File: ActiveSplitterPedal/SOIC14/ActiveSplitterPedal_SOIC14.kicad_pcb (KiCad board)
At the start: 2 copper layers, 124 x 100.8 mm, 78 parts, among them J1 MonoJack2Switch, J2 MonoJack2Switch, J3 MonoJack2Switch, J4 MonoJack2Switch, J5 MonoJack2Switch, J6 Barrel_Jack, U1 TL074, U2 TL074, U3 TL074, U4 TL074, U5 TPS60400, U6 TPS60400, U7 TPS60400, U8 TPS60400, U9 SE8250X2

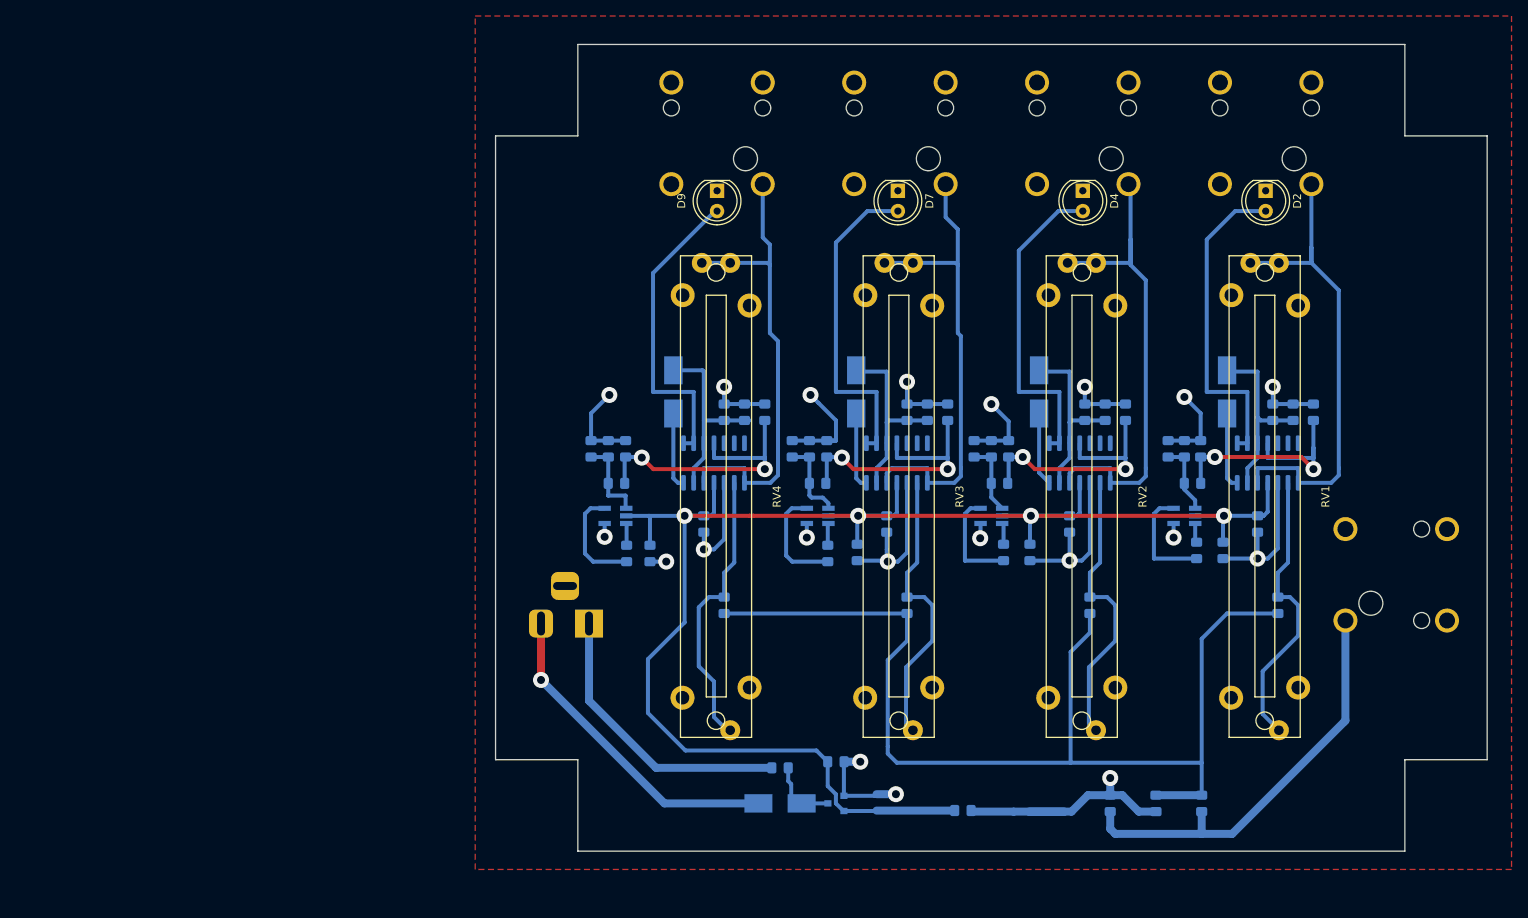
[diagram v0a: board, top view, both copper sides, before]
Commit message: Adjusted layout edges using Hammond 1590BB outline
- Moved components to fit within reduced board area
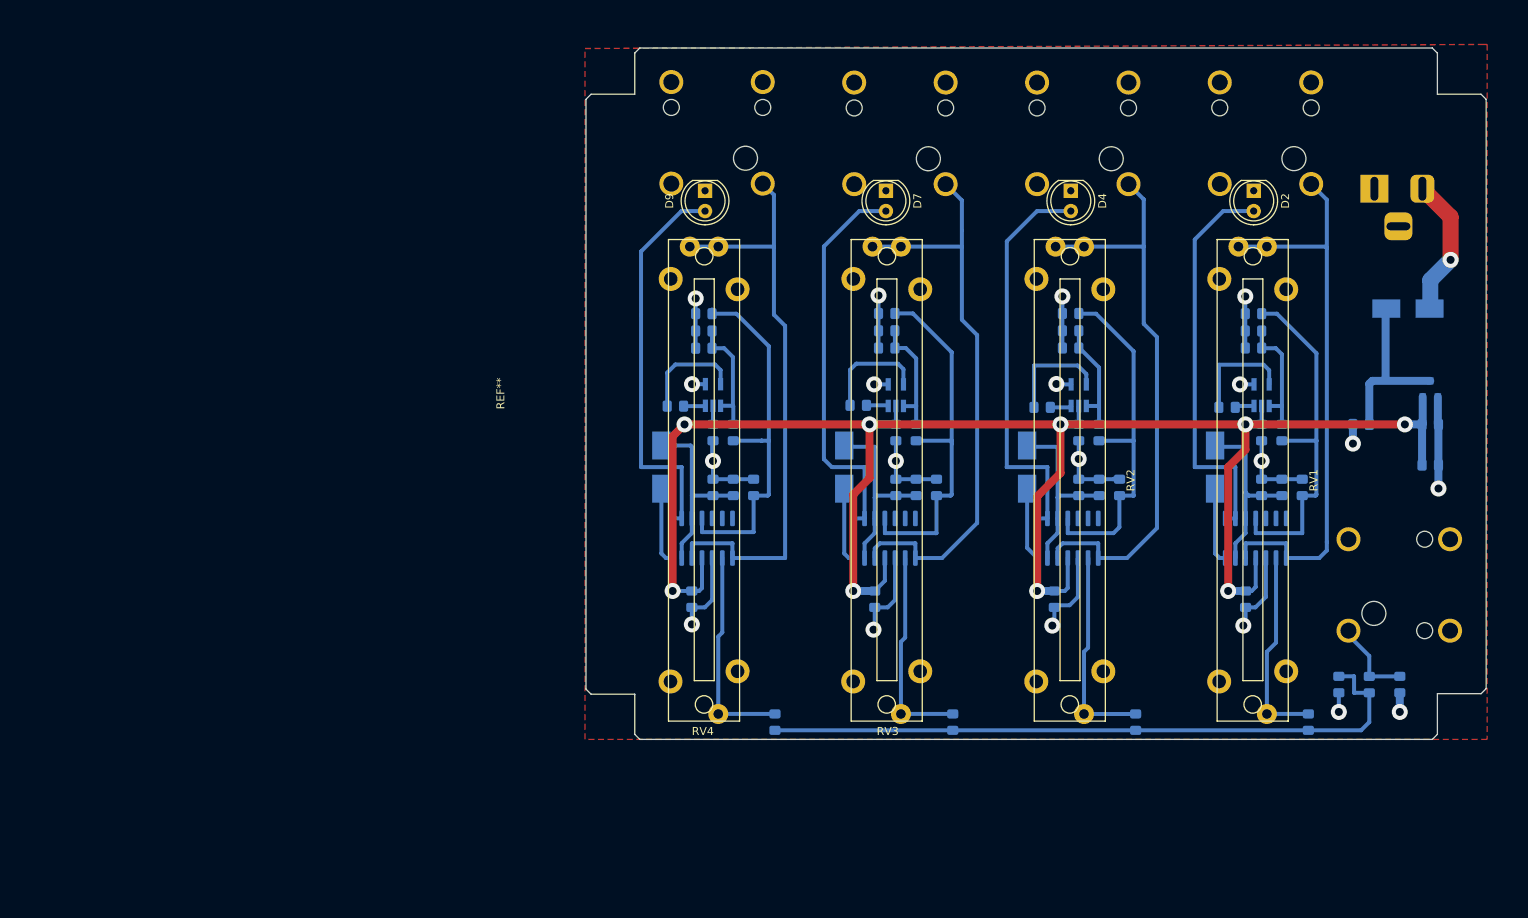
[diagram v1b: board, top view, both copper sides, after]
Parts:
- added REF**: 1590BB, Hammond1590:1590BB, F.Cu at (207.3, 67.6)
- moved J6 112.2 mm to (249.6, 41.9), turned to 180 degrees
- moved D5 99.9 mm to (253.7, 56.9), turned to 0 degrees
- moved U9 90.6 mm to (256.5, 66.9), turned to 90 degrees
- moved C5 84.4 mm to (247.9, 71.4)
- moved C8 83.0 mm to (256.5, 76.5)
- moved C10 75.8 mm to (256.5, 71.4)
- moved R6 39.1 mm to (252.7, 103.9), turned to 270 degrees
- moved R7 27.3 mm to (245.1, 103.9)
- moved R5 25.7 mm to (248.9, 103.9), turned to 90 degrees
- moved C28 19.5 mm to (165.7, 57.5), turned to 180 degrees
- moved U7 19.4 mm to (166.9, 67.7), turned to 90 degrees
- moved C26 19.4 mm to (162.2, 69.1), turned to 180 degrees
- moved C27 19.0 mm to (165.7, 59.7), turned to 180 degrees
- moved C22 18.9 mm to (185.0, 69.0), turned to 180 degrees
- moved C34 18.9 mm to (165.7, 61.8), turned to 180 degrees
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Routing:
- net GNDS: track 233.9 -> 133.5 mm
- net /GainAndPeakDetector1/SIGNAL_INPUT: track 136.7 -> 84.2 mm
- net Net-(J5-Pad1): track 53.0 -> 9.97 mm
- net +5V: track 208.7 -> 238.2 mm, vias 4 -> 9
- net /PowerSupply/+9V_IN: track 40.8 -> 17.1 mm
- net /GainAndPeakDetector4/SIGNAL_OUTPUT: track 59.1 -> 73.8 mm
- net /GainAndPeakDetector3/SIGNAL_OUTPUT: track 59.7 -> 73.3 mm
- net /GainAndPeakDetector2/-5V_POL: track 32.2 -> 45.5 mm, vias 2 -> 0
- net /GainAndPeakDetector3/-5V_POL: track 33.4 -> 46.4 mm, vias 2 -> 0
- net /PowerSupply/+9V_POL: track 9.19 -> 21.7 mm
- net /GainAndPeakDetector1/-5V_POL: track 32.9 -> 45.0 mm, vias 2 -> 0
- net /GainAndPeakDetector2/SIGNAL_OUTPUT: track 61.4 -> 72.7 mm
- net /GainAndPeakDetector4/-5V_POL: track 35.7 -> 46.7 mm, vias 2 -> 0
- net Net-(D9-Pad2): track 38.8 -> 49.8 mm
- net Net-(R1-Pad1): track 36.1 -> 25.2 mm
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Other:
- board size 124 x 100.8 mm -> 112.5 x 86.4 mm

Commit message: updated
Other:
- board text added: "Active 4-Way Splitter RevA"
- board text removed: "Active 4-Way Splitter Hammond 1590BB"

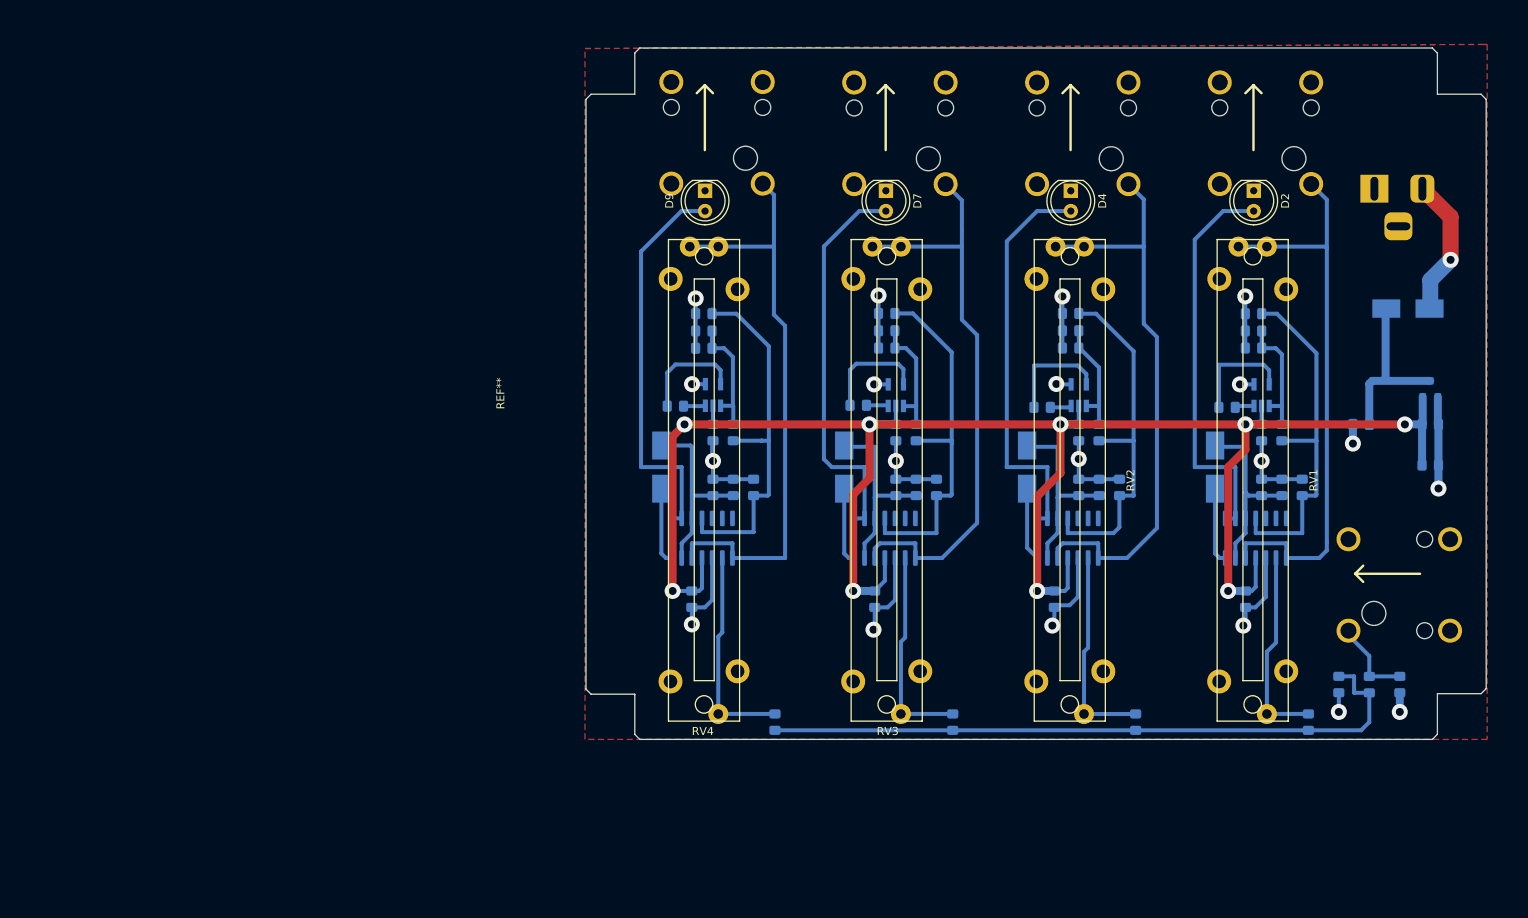
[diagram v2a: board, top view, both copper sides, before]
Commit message: updated RevA layout
Moved components so that faders would be in centred and symmetrical positions
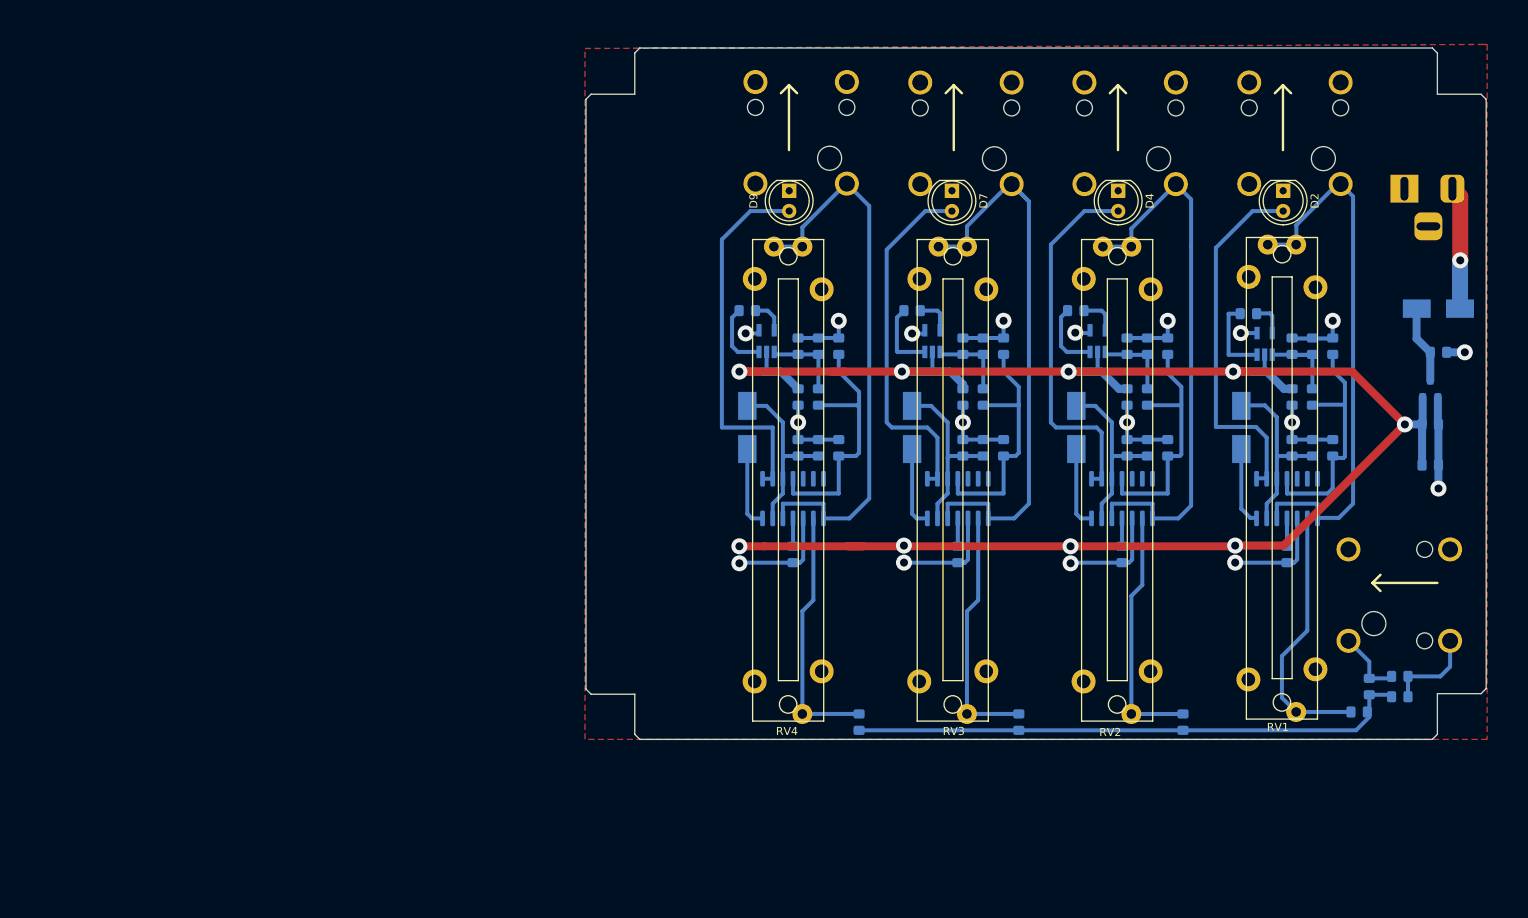
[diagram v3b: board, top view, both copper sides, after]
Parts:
- removed REF**: 1590BB, Hammond1590:1590BB
- moved C28 17.3 mm to (182.6, 61.6), turned to 90 degrees
- moved C24 15.2 mm to (203.2, 61.6), turned to 90 degrees
- moved C26 14.9 mm to (171.2, 57.1), turned to 0 degrees
- moved C27 14.5 mm to (180.1, 61.6), turned to 90 degrees
- moved C18 13.8 mm to (176.9, 87.6)
- moved C22 13.6 mm to (191.8, 57.1), turned to 0 degrees
- moved C5 13.2 mm to (257.6, 62.4), turned to 0 degrees
- moved C11 12.8 mm to (223.7, 61.6), turned to 90 degrees
- moved C2 12.8 mm to (212.2, 57.1), turned to 0 degrees
- moved U4 12.4 mm to (176.9, 80.6)
- moved C33 12.2 mm to (200.7, 61.6), turned to 90 degrees
- moved C30 12.0 mm to (233.8, 57.5), turned to 0 degrees
- moved D6 11.8 mm to (171.2, 71.8)
- moved C15 11.8 mm to (197.5, 87.6)
- moved C34 11.8 mm to (177.5, 61.6), turned to 90 degrees
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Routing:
- net +5V: track 238.2 -> 278.0 mm
- net GNDS: track 133.5 -> 151.3 mm, vias 20 -> 18
- net /GainAndPeakDetector3/-5V_POL: track 46.4 -> 31.9 mm
- net /GainAndPeakDetector1/SIGNAL_INPUT: track 84.2 -> 69.9 mm
- net /GainAndPeakDetector1/-5V_POL: track 45.0 -> 30.8 mm
- net /GainAndPeakDetector2/-5V_POL: track 45.5 -> 31.5 mm
- net /GainAndPeakDetector4/-5V_POL: track 46.7 -> 33.5 mm
- net /PowerSupply/+9V_POL: track 21.7 -> 9.64 mm
- net Net-(C30-Pad2): track 13.7 -> 4.38 mm
- net Net-(C26-Pad2): track 13.3 -> 4.32 mm
- net Net-(C22-Pad2): track 13.6 -> 4.74 mm
- net Net-(C2-Pad2): track 13.5 -> 4.86 mm
- net Net-(R1-Pad1): track 25.2 -> 33.2 mm
- net Net-(C30-Pad1): track 2.42 -> 10.2 mm
- net Net-(C22-Pad1): track 2.76 -> 8.97 mm
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
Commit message: added uv etch layout
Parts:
- D5: footprint Diode_SMD:D_SMB_Handsoldering -> Diode_SMD:D_SOD-123F
- moved D5 1.30 mm to (258.8, 56.6)
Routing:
- net /PowerSupply/+9V_IN: track 15.4 -> 18.7 mm

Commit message: updated reva layout
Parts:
- moved R1 91.5 mm to (158.8, 128.9), turned to 270 degrees
- moved R11 90.3 mm to (97.2, 128.9)
- moved R3 90.2 mm to (137.8, 128.9)
- moved R9 90.0 mm to (117.5, 128.9)
- moved C15 77.0 mm to (123.2, 108.0)
- moved C4 76.9 mm to (164.5, 108.0)
- moved C18 76.8 mm to (102.9, 108.0)
- moved C12 76.6 mm to (144.1, 108.0)
- moved C2 74.1 mm to (141.1, 77.9)
- moved C22 74.1 mm to (120.7, 77.9)
- moved C26 74.1 mm to (100.1, 77.9)
- moved U6 74.1 mm to (123.2, 81.7)
- moved U7 74.1 mm to (102.5, 81.7)
- moved U5 74.1 mm to (143.8, 81.7)
- moved C10 74.0 mm to (185.4, 91.7)
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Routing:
- net Net-(R9-Pad1): track 31.5 -> 91.0 mm, vias 0 -> 2
- net Net-(R11-Pad1): track 32.1 -> 91.2 mm, vias 0 -> 2
- net Net-(R3-Pad1): track 31.5 -> 90.0 mm, vias 0 -> 2
- net Net-(R1-Pad1): track 33.2 -> 91.6 mm, vias 0 -> 2
- net /GainAndPeakDetector1/SIGNAL_INPUT: track 69.9 -> 87.0 mm
- net /GainAndPeakDetector2/SIGNAL_OUTPUT: track 68.9 -> 85.1 mm
- net /GainAndPeakDetector3/SIGNAL_OUTPUT: track 72.2 -> 88.3 mm
- net /GainAndPeakDetector1/SIGNAL_OUTPUT: track 68.3 -> 83.9 mm
- net /GainAndPeakDetector4/SIGNAL_OUTPUT: track 69.8 -> 85.1 mm
- net Net-(D7-Pad2): track 45.3 -> 50.6 mm
- net Net-(D2-Pad2): track 46.0 -> 51.0 mm
- net Net-(D4-Pad2): track 46.3 -> 51.1 mm
- net Net-(D9-Pad2): track 47.4 -> 51.8 mm
- net +5V: track 278.0 -> 274.9 mm
- net /GainAndPeakDetector4/-5V_POL: track 33.5 -> 31.5 mm
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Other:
- board text added: "Do not mirror if etching."
